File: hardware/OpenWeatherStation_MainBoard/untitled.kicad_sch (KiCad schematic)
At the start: 1 part, among them J1 RJ45_LED_Shielded

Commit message: poe design wip
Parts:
- added C1, C14, C15, C2, C3, C4, C6, C8, C9: 1nF, symbol Device:C
- added C10, C12, C13, C16, C19: 0.1uF, symbol Device:C
- added C11: 22uF, symbol Device:C_Polarized
- added C17, C18: 470pF, symbol Device:C
- added C20, C7: 1uF, symbol Device:C
- added C5: 2.2nF, symbol Device:C
- added D1, D2: DF01S1, Diode_SMD:Diode_Bridge_OnSemi_SDIP-4L, symbol Diode_Bridge:DF01S1
- added D3: SMAJ58A, Diode_SMD:D_SMA, symbol Diode:SMAJ58A
- added D4, D6: D, symbol Device:D
- added D5: LED, symbol Device:LED
- added L1: L, symbol Device:L
- added Q1: Q_NMOS_GDS, symbol Device:Q_NMOS_GDS
- added R10: 52R, symbol Device:R
- added R11, R12, R13: 0.33R, symbol Device:R
- added R14: 10k, symbol Device:R
- added R15: 510R, symbol Device:R
- added R16: 4k7, symbol Device:R
- added R17, R8: 10R, symbol Device:R
- added R2: 0R0, symbol Device:R
- added R3, R4, R5, R6: R, symbol Device:R
- added R7: 22k, symbol Device:R
- added R9: 124k, symbol Device:R
- added U4: ~, symbol New_Library:SM13126PEL
- added U5: PM8800A, symbol New_Library:PM8800A
- added U6: POE13P-33L, symbol New_Library:POE13P-33L
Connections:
- net GNDPWR: now also C5.2
- net at J1.1: now also U4.16 (TX1+)
- net at J1.2: now also U4.14 (TX1-)
- net at J1.3: now also U4.11 (TX2+)
- net at J1.4: now also J1.5, D1.4, R3.1
- net at J1.6: now also U4.9 (TX2-)
- net at J1.7: now also J1.8, D1.3, R4.1
- new net: R9.1, U5. (nPGD)
- new net: C16.1, R9.2, U5. (nPGD)
- new net: D2.3, R5.1, U4.15 (CT1)
- new net: C2.1, R5.2
- new net: C3.1, R4.2
- new net: C19.1, C20.1, D6.1 (K), R16.2, U5. (nPGD)
- new net: D4.2 (A), Q1.1 (G), R12.1, R14.2
- new net: C13.1, L1.2, R8.1, U6.3
- new net: C15.2, R8.2, U5. (nPGD)
- new net: Q1.3 (S), R11.2, R15.1
- new net: C17.1, R15.2, U5. (nPGD)
- new net: Q1.2 (D), U6.4
- new net: R17.2, U6.2
- new net: U6.5, U6.6
- new net: U6.7, U6.8
- new net: R2.1, U4.2 (CT1)
- new net: R2.2, U4.7 (CT2)
- new net: R10.1, U5. (nPGD)
- new net: D4.1 (K), R13.1
- new net: R12.2, R13.2, U5. (nPGD)
- new net: C1.2, C2.2, C3.2, C4.2, C5.1
- new net: C4.1, R3.2
- new net: C16.2, U5. (nPGD)
- new net: D2.4, R6.1, U4.10 (CT2)
- new net: D6.2 (A), R17.1
- new net: C18.1, D5.1 (K), U5. (nPGD)
- new net: R7.1, U5. (nPGD)
- new net: C1.1, R6.2
- new net: D5.2 (A), R16.1
- new net GND: C10.2, C11.2, C12.2, C13.2, C14.2, C17.2, C20.2, C8.2, C9.1, R11.1, R14.1, U5. (nPGD), U6.1
- new net GNDA: C18.2, C19.2
- new net POE_F: C10.1, C11.1, C12.1, C6.1, C7.1, C8.1, D1.1 (+), D2.1 (+), D3.1 (A1), L1.1
- new net VSS: C14.1, C15.1, C6.2, C7.2, C9.2, D1.2 (-), D2.2 (-), D3.2 (A2), R10.2, R7.2, U5. (nPGD)
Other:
- moved on the sheet: J1

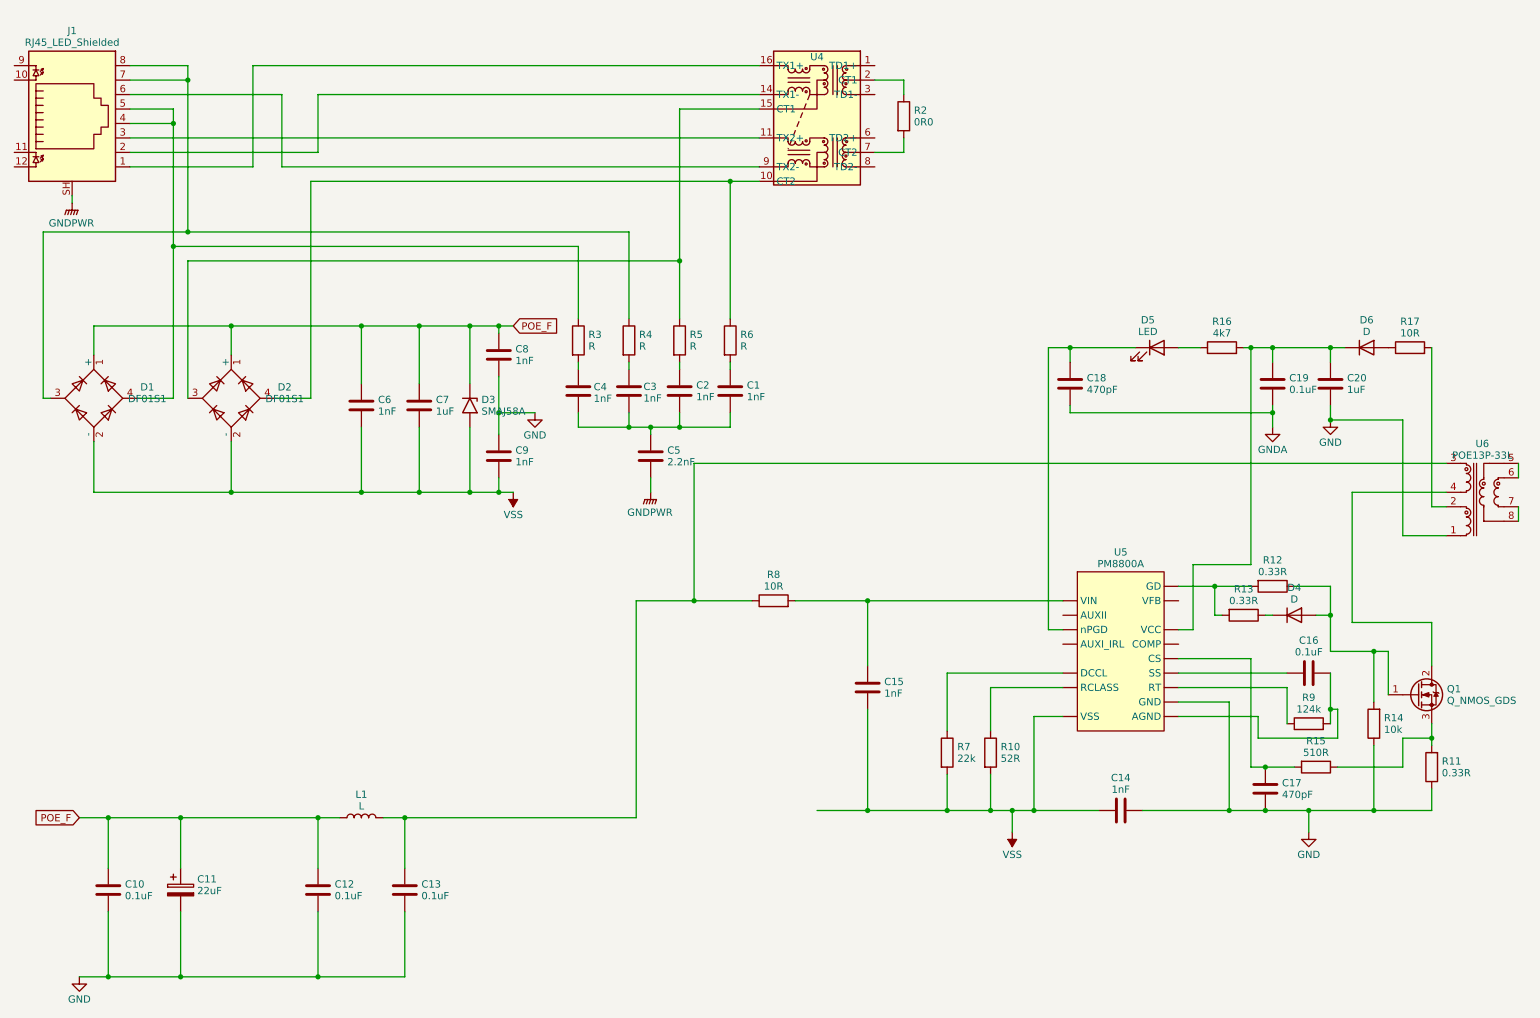
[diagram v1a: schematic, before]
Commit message: update board schematics (sensors, ethernet ...)
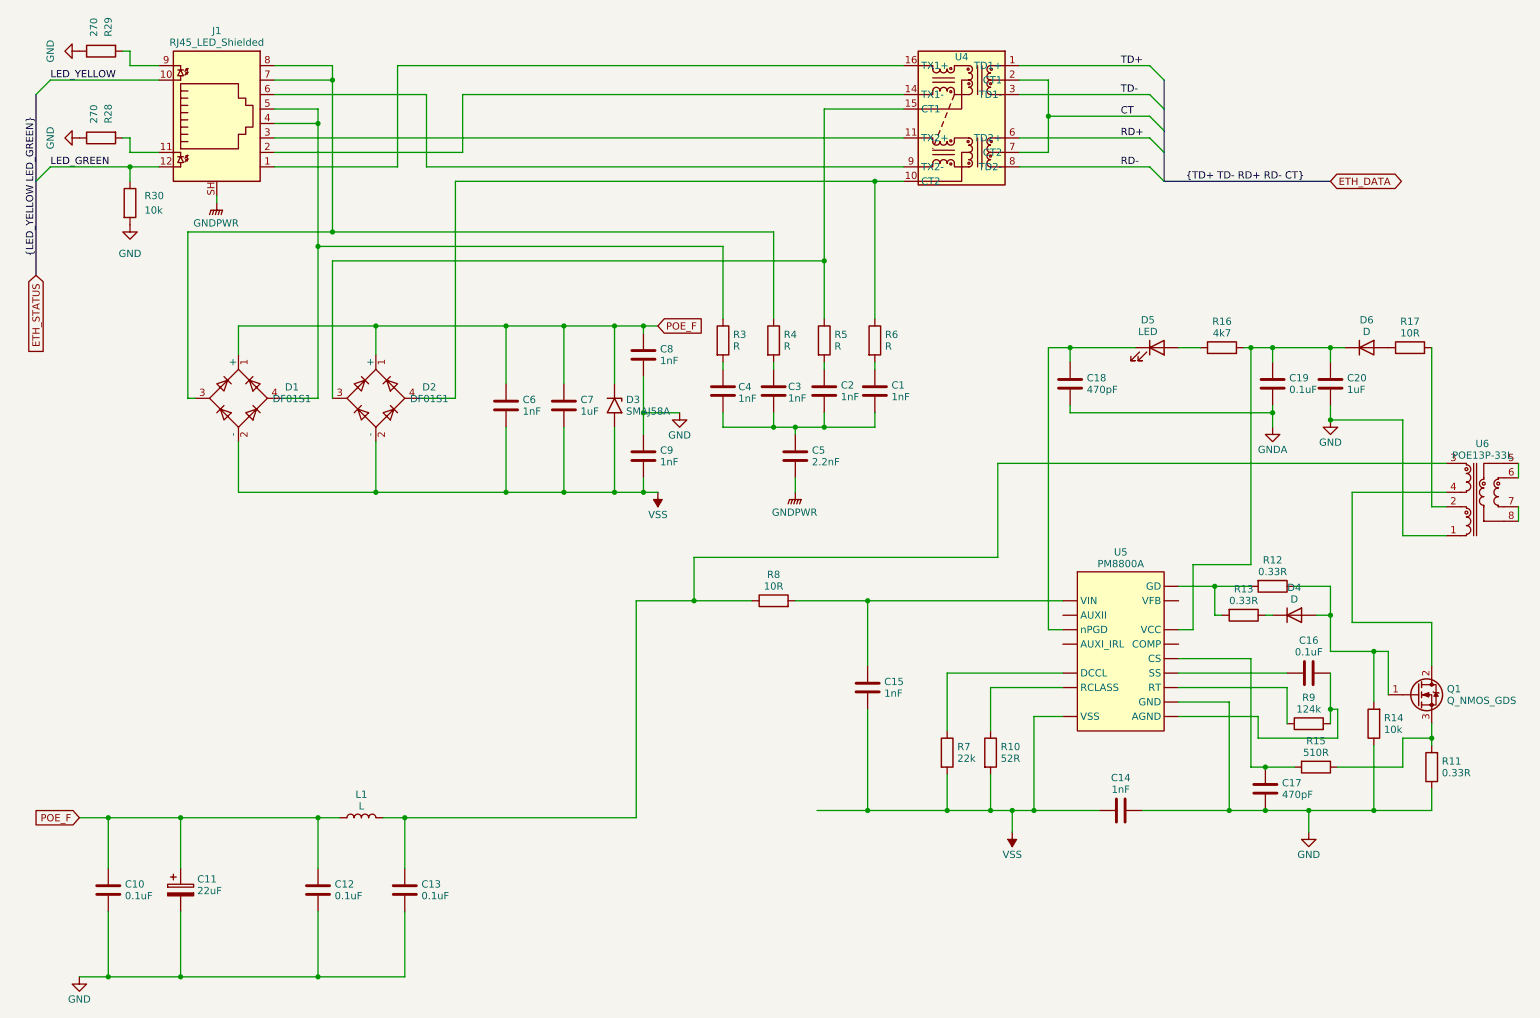
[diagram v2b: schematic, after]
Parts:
- removed R2: 0R0, symbol Device:R
- added R28, R29: 270, symbol Device:R
- added R30: 10k, symbol Device:R
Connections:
- net GND: now also R28.1, R29.1, R30.2
- net CT: now reaches U4.2 (CT1)
- net CT: now also U4.7 (CT2)
- net TD+: now reaches U4.1 (TD1+)
- net TD-: now reaches U4.3 (TD1-)
- net RD+: now reaches U4.6 (TD2+)
- net RD-: now reaches U4.8 (TD2-)
- net LED_YELLOW: now reaches J1.10
- net at J1.11: now also R28.2
- net LED_GREEN: now reaches J1.12
- net LED_GREEN: now also R30.1
- net at J1.9: now also R29.2
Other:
- moved on the sheet: C1, C2, C3, C4, C5, C6, C7, C8, C9, D1, D2, D3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

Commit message: fix hierarchical bus
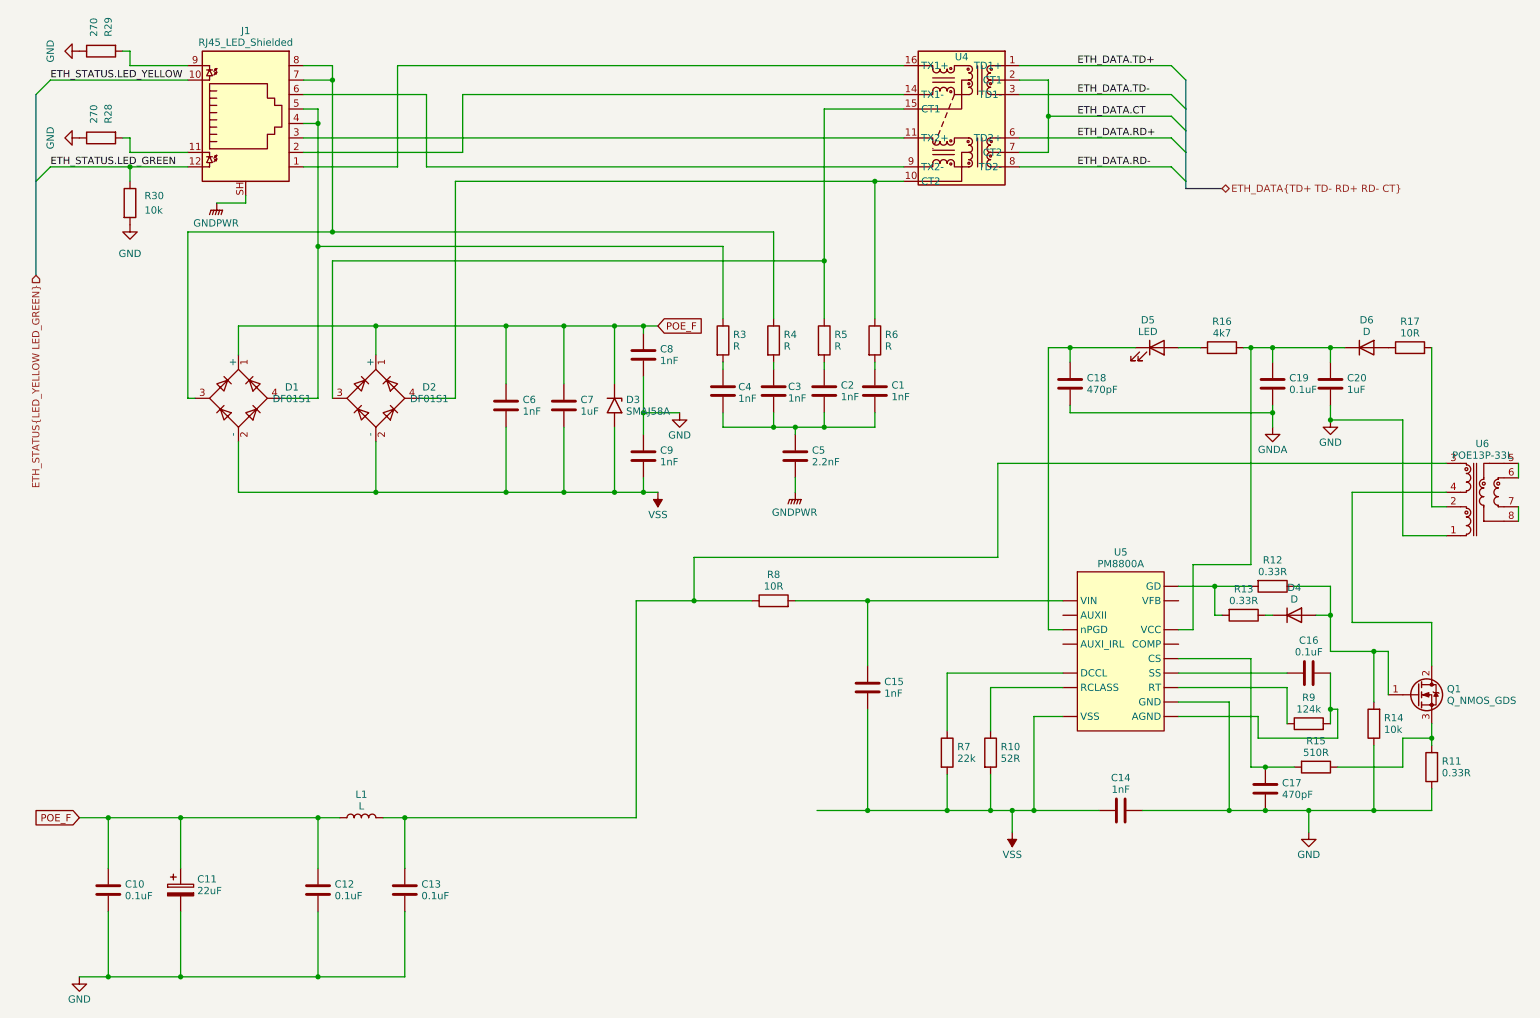
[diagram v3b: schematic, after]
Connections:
- net CT renamed ETH_DATA.CT
- net LED_GREEN renamed ETH_STATUS.LED_GREEN
- net LED_YELLOW renamed ETH_STATUS.LED_YELLOW
- net RD+ renamed ETH_DATA.RD+
- net RD- renamed ETH_DATA.RD-
- net TD+ renamed ETH_DATA.TD+
- net TD- renamed ETH_DATA.TD-
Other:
- moved on the sheet: J1
